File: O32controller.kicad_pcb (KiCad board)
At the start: 4 copper layers, 27 x 27 mm, 81 parts, among them J1 SWD, J10 3V3, J11 GND, J12 I2C/RS485_2, J2 BATT+, J3 BATT-, J4 Motor Connection, J5 Motor Connection, J6 Motor Connection, J7 BATT+, J8 BATT-, J9 I2C/RS485_1, Q1 CSD88584Q5DCT, Q2 CSD88584Q5DCT, Q3 CSD88584Q5DCT, SW1 RESET, U1 MA702GQ-P, U2 STSPIN32F0A, U3 THVD1420DRLR

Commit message: woohoo everything connected, no drc err
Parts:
- added R30: 27.4k, Resistor_SMD:R_0402_1005Metric, B.Cu at (47.9, 55.3)
- added R31: 27.4k, Resistor_SMD:R_0402_1005Metric, B.Cu at (45.8, 55.6)
- added R32: 27.4k, Resistor_SMD:R_0402_1005Metric, B.Cu at (43.7, 49.2)
- added R33: 27.4k, Resistor_SMD:R_0402_1005Metric, B.Cu at (43.7, 48.3)
- added R34: 27.4k, Resistor_SMD:R_0402_1005Metric, B.Cu at (42.1, 46.2)
- added R35: 27.4k, Resistor_SMD:R_0402_1005Metric, B.Cu at (43.1, 46.2)
- D1: value SBA0540Q -> SDM2U30CSP; footprint Diode_SMD:D_DFN2L -> O32controller:SDM2U30CSP-7
- D5, D6: value PMEG4010ESB -> SDM2U30CSP
- J10, J11: footprint Connector_Wire:SolderWire-0.1sqmm_1x01_D0.4mm_OD1mm -> O32controller:SolderWire-Actual_1x01_D1.25mm_OD_2.3mm
- NT4, NT5, TP2, U3: moved to B.Cu
- R1, R5, R9: value WFCP06124L000FE66 0.004R -> WSLF25122L000FEB 0.002R
- moved R29 25.3 mm to (38.5, 42.3), turned to 90 degrees
- moved TP2 23.1 mm to (44.0, 58.4), turned to 180 degrees
- moved NT4 20.7 mm to (43.0, 43.6), turned to 180 degrees
- moved NT5 19.6 mm to (43.0, 42.6), turned to 180 degrees
- moved D6 18.3 mm to (39.4, 45.9), turned to 180 degrees
- moved D5 17.8 mm to (37.5, 47.5), turned to 90 degrees
- moved J10 15.7 mm to (41.5, 59.5)
- moved J11 15.6 mm to (41.5, 62.1)
- moved D2 10.8 mm to (53.9, 37.9), turned to -90 degrees
- moved U3 6.26 mm to (42.0, 50.9), turned to 90 degrees
- moved J9 5.80 mm to (39.5, 43.1)
- moved D1 5.03 mm to (40.7, 55.2), turned to -90 degrees
- moved D3 4.99 mm to (37.2, 45.0), turned to 90 degrees
- moved J12 4.65 mm to (39.5, 48.5)
- moved R28 3.52 mm to (38.5, 44.4), turned to 90 degrees
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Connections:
- net /USART1_DE renamed /USART_DE
- net Net-(D3-Pad2) renamed /Red_Anode
- net Net-(D4-Pad1) renamed /Green_Cathode
- net USART1_TX renamed USART_TX
- U3 pad 1: /USART1_RX -> /USART_RX
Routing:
- net +3.3V: track 2.68 -> 61.6 mm, vias 0 -> 7
- net GND: track 11.8 -> 37.0 mm, vias 12 -> 33
- net VBUS: track 1.62 -> 24.2 mm, vias 2 -> 4
- net SWD_IO: track 1.81 -> 15.6 mm
- net /RS485_B: track 0.00 -> 12.5 mm, vias 0 -> 2
- net USART_TX: track 0.00 -> 11.8 mm, vias 0 -> 1
- net /NRST: track 0.00 -> 11.8 mm, vias 0 -> 2
- net SWD_CLK: track 0.66 -> 12.2 mm
- net /RS485_A: track 0.00 -> 10.9 mm
- net /SW_3.3: track 0.00 -> 8.05 mm
- net /LED_STATUS: track 0.00 -> 6.93 mm
- net /USART_RX: track 1.11 -> 6.92 mm
- net I2C_SCL: track 0.00 -> 5.63 mm
- net /BUS_SENSE: track 0.00 -> 5.48 mm, vias 0 -> 1
- net /OP_V_O: track 3.31 -> 8.47 mm
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- added copper zone on In1.Cu, net GND

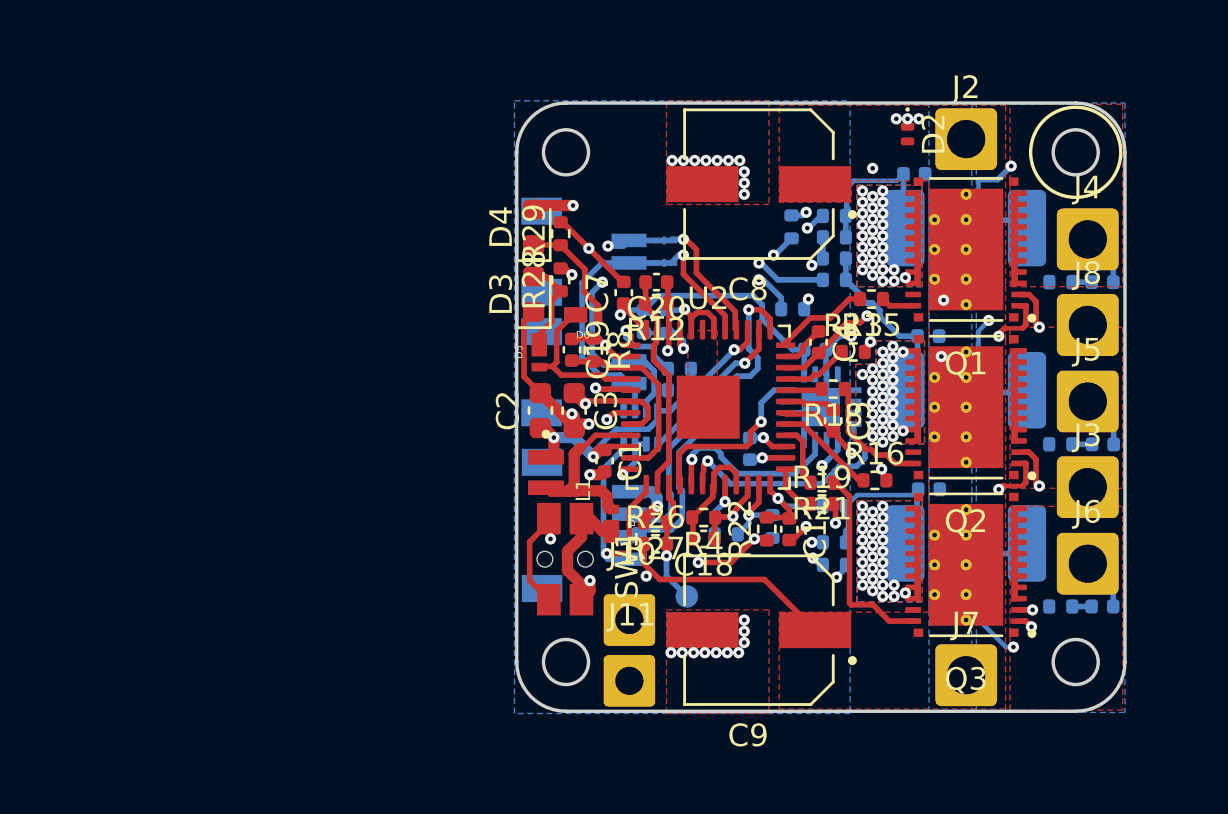
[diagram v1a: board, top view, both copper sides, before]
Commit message: choose led, tvs, start on silkscreen
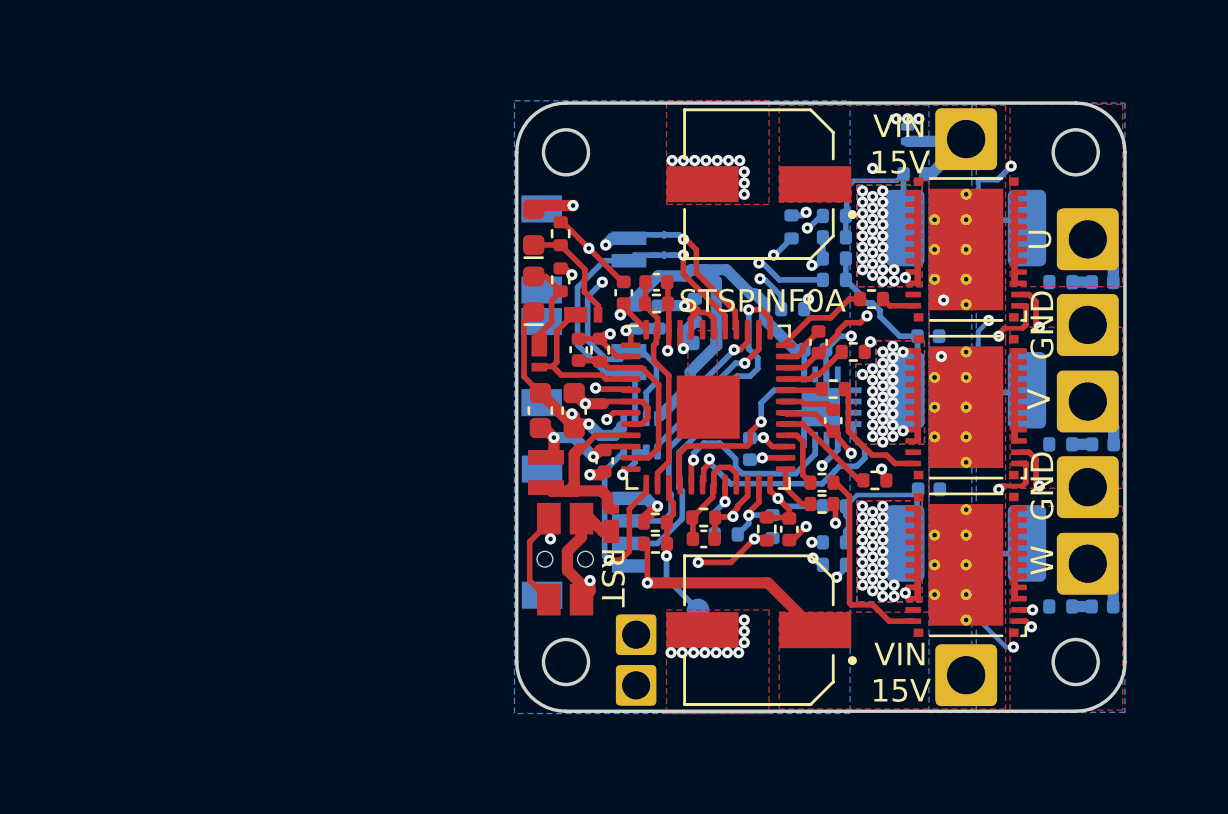
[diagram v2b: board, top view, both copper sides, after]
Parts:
- D2: moved to B.Cu
- J10, J11: footprint O32controller:SolderWire-Actual_1x01_D1.25mm_OD_2.3mm -> O32controller:SolderWire-Actual_1x01_D1.25mm_OD_1.8mm
- Q1, Q2, Q3: value CSD88584Q5DCT -> DMM0022A
- U1: value MA702GQ-P -> QFN-3x3_MA702_MNP
- moved R32 3.77 mm to (41.8, 46.0), turned to 90 degrees
- moved R34 2.86 mm to (44.9, 47.1), turned to 0 degrees
- moved R33 2.48 mm to (42.8, 46.0), turned to -90 degrees
- moved R35 1.35 mm to (44.4, 45.7)
- moved BUS_SENSE 0.78 mm to (44.5, 59.0)
- moved J10 0.72 mm to (41.8, 60.1)
- moved J12 0.45 mm to (39.5, 48.0)
- moved J11 0.36 mm to (41.8, 62.4)
- moved NT4 0.35 mm to (43.0, 43.2)
- moved U3 0.35 mm to (42.0, 51.2)
- moved R8 0.30 mm to (40.2, 47.5)
- moved C19 0.30 mm to (39.2, 47.5)
- moved J1 0.30 mm to (41.5, 55.5)
- moved NT5 0.25 mm to (43.0, 42.4)
- moved J9 0.10 mm to (39.5, 43.0)
- renumbered TP2 to BUS_SENSE, SW1 to RST, U2 to STSPINF0A
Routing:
- net VBUS: track 24.2 -> 30.0 mm
- net +3.3V: track 61.6 -> 64.6 mm
- net GND: track 37.0 -> 39.9 mm
- net /OP_V_P: track 15.0 -> 12.5 mm
- net /Motor phase U/Motor: track 3.98 -> 2.37 mm
- net USART_TX: track 11.8 -> 10.6 mm
- net /RS485_B: track 12.5 -> 13.4 mm
- net /OP_W_P: track 17.0 -> 16.2 mm
- net /BUS_SENSE: track 5.48 -> 6.29 mm
- net /RS485_A: track 10.9 -> 11.6 mm
- net /OC_COMP: track 18.0 -> 18.6 mm
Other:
- board text added: "GND"
- board text added: "U"
- board text added: "V"
- board text added: "VIN 15V"
- board text added: "W"

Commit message: silkscreen pretty much done
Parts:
- U1: value QFN-3x3_MA702_MNP -> MA702
- renumbered U3 to RS485, BUS_SENSE to SNS
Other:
- board text added: "+"
- board text added: "-"
- board text added: "2mΩ 5W"
- board text added: "3.3"
- board text added: "CLK"
- board text added: "I2C,RS485"
- board text added: "IO"
- board text added: "M2"
- board text added: "SCL,B"
- board text added: "SDA,A"
- board text added: "TX"
- board text added: "VIN"
- board text added: "VIN: 7-15V"
- board text added: "Ø32"
- board text removed: "VIN 15V"

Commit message: finish, generate gerbers
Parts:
- added C21: 1nF, Capacitor_SMD:C_0402_1005Metric, B.Cu at (45.8, 56.6)
- Q1, Q2, Q3: value DMM0022A -> CSD88584Q5DCT
- R26: value 40k -> 41.2k
- renumbered RS485 to U3
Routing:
- net /BUS_SENSE: track 6.29 -> 8.69 mm
- net /Motor phase U/Sense_N: track 15.1 -> 14.5 mm, vias 3 -> 2
- net GND: track 39.9 -> 39.6 mm, vias 33 -> 51
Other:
- board text added: "16AWG"
- board text added: "3.3V"
- board text added: "JST"
- board text added: "SH"
- board text added: "[1/6/23]"
- board text added: "v2"
- board text removed: "3.3"

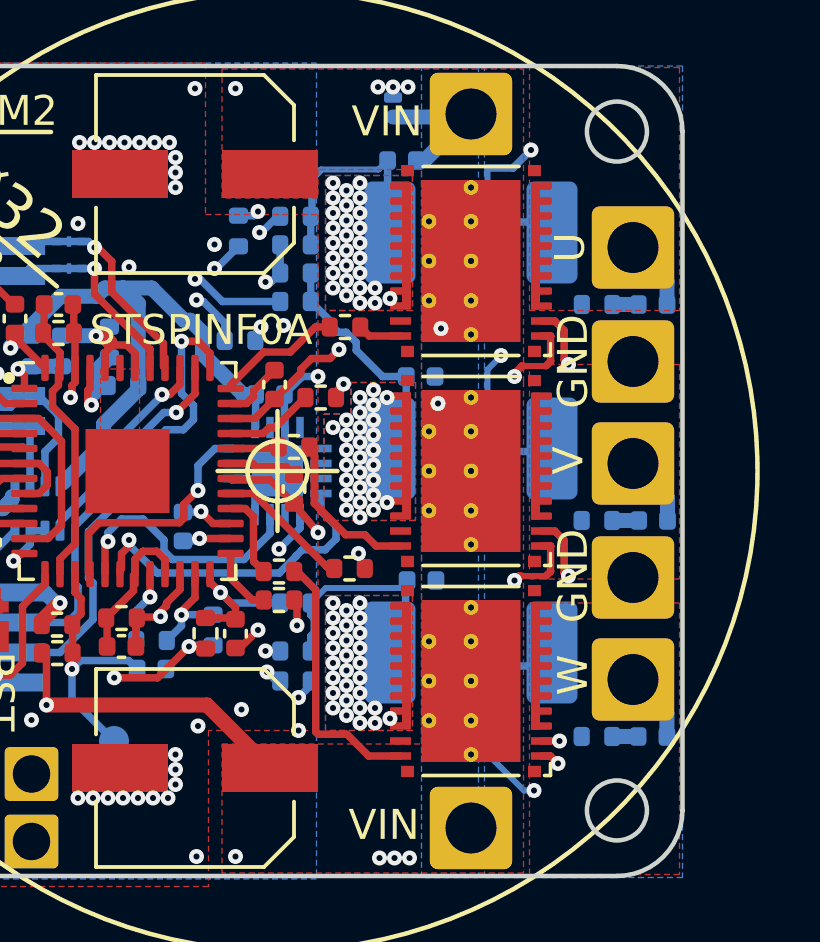
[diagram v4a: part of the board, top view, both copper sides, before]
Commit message: fix mosfet soldermask
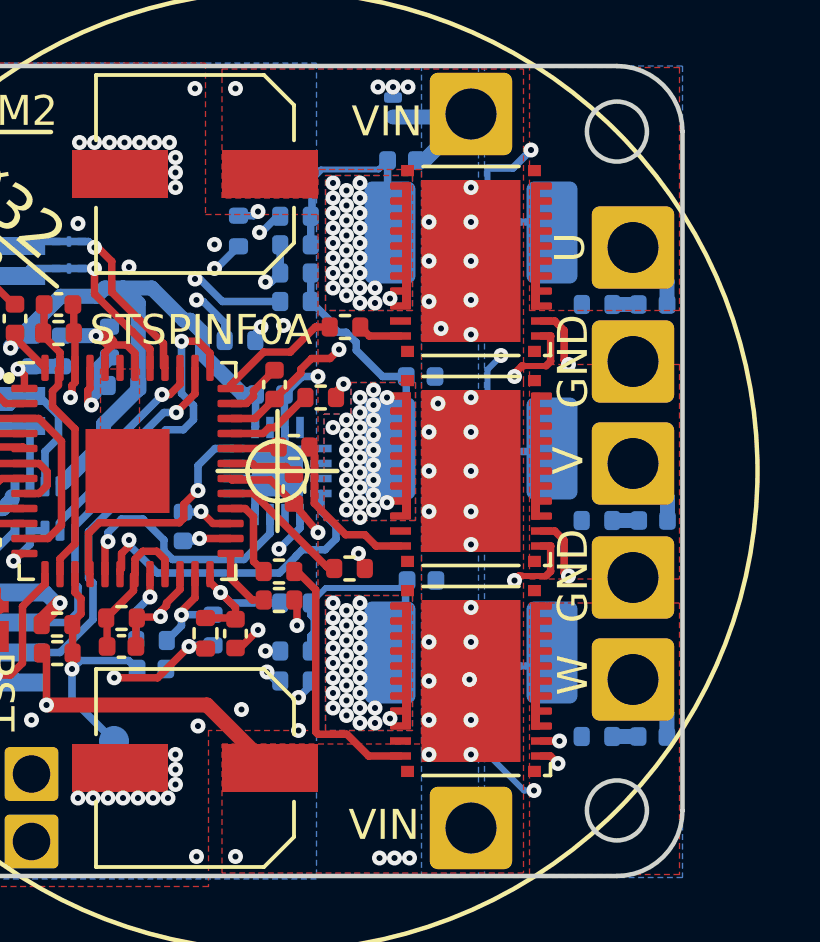
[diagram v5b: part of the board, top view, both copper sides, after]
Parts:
- Q1, Q2, Q3: value CSD88584Q5DCT -> DMM0022A
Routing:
- net VBUS: vias 4 -> 29

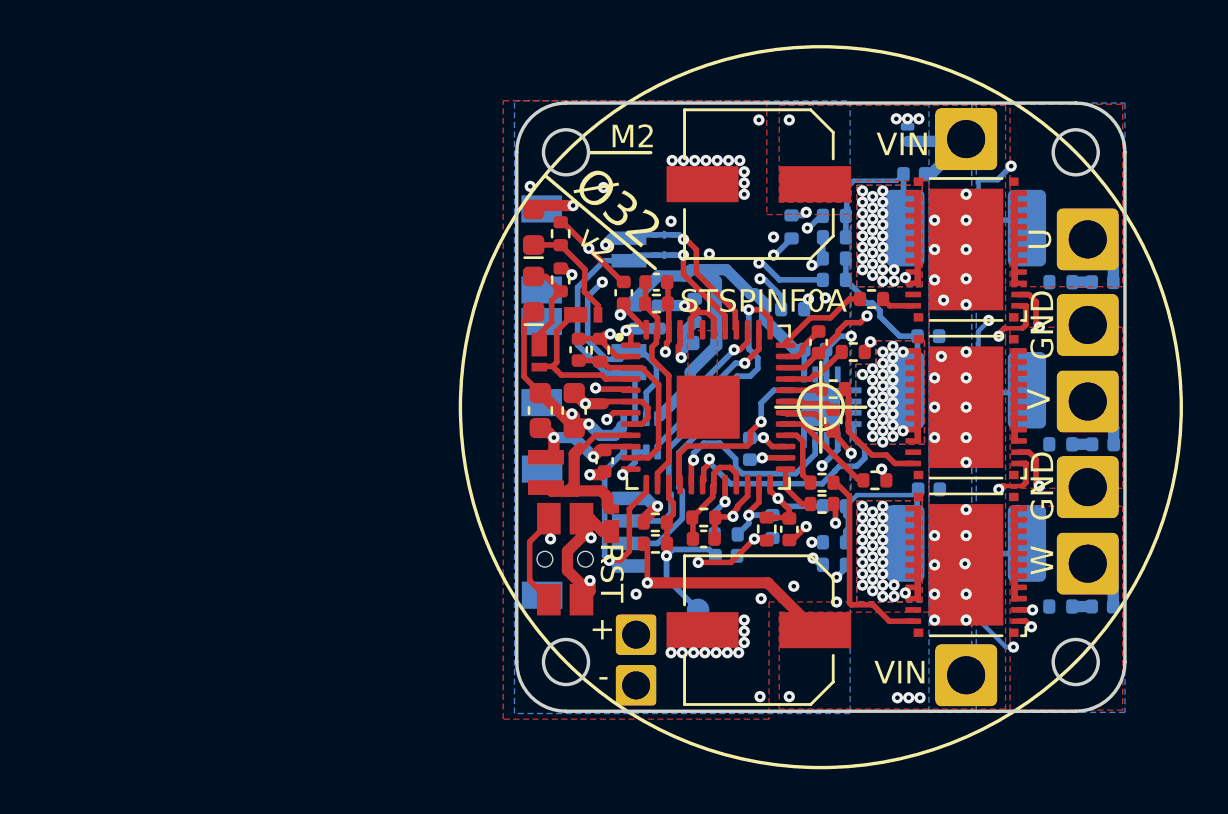
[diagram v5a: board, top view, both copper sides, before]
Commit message: clean up v2, fix libraries, netties, fix TVS dir
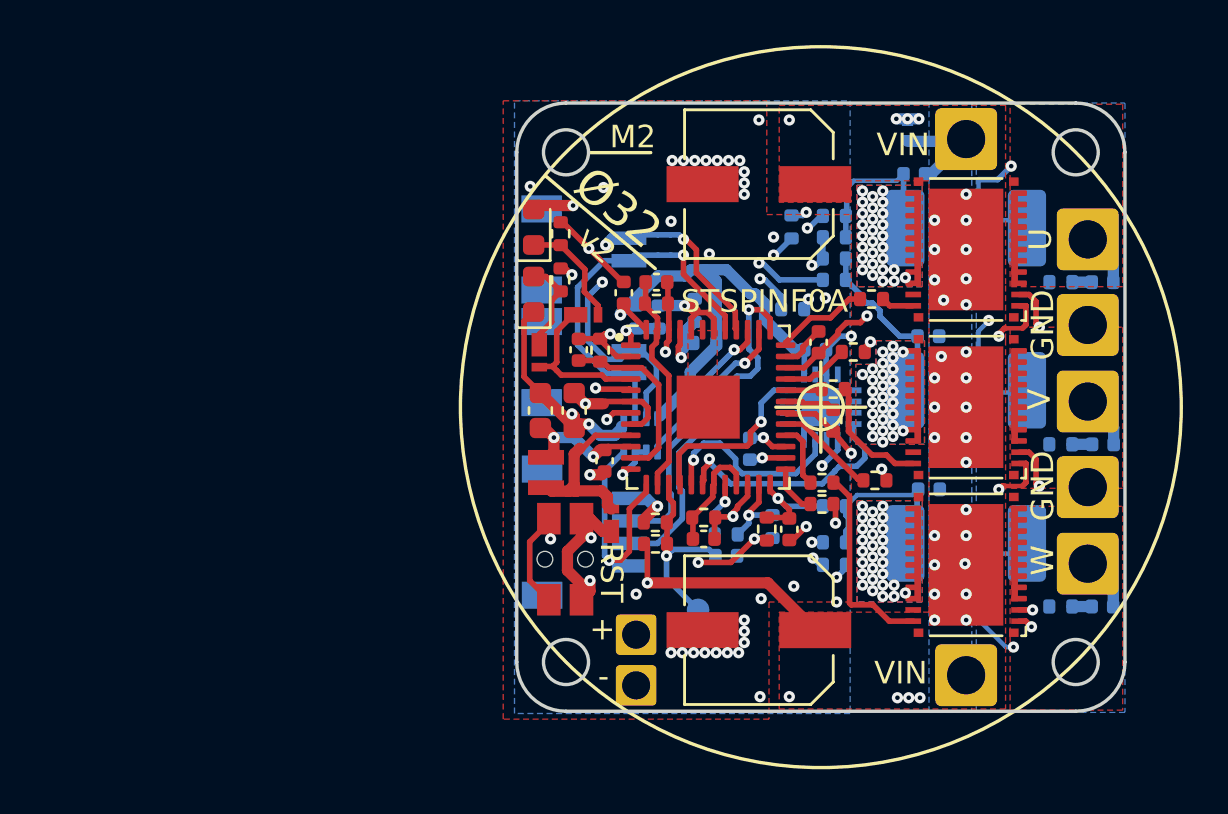
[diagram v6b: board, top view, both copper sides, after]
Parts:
- removed D2: ESDA17P20-1F2, Diode_SMD:D_0402_CSP
- added CR1: ESDA17P20-1F2, O32controller:SMT2_0P91X0P63_STM-L, B.Cu at (53.9, 37.7)
- NT1, NT2, NT3, NT4, NT5: footprint NetTie:NetTie-small -> O32controller:NetTie-2_SMD_Pad0.25mm
- R1, R5, R9: footprint Resistor_SMD:R_Shunt_2512_6332Metric -> O32controller:R_Shunt_2512_6332Metric
- U1: value MA702 -> QFN-3x3_MA702_MNP
- moved NT3 0.45 mm to (57.4, 56.5)
- moved NT1 0.40 mm to (57.4, 41.7)
- moved NT2 0.35 mm to (57.4, 49.4)
- renumbered RST to SW1, SNS to TP2, STSPINF0A to U2
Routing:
- net GND: track 39.6 -> 45.4 mm
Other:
- board text added: "MA702"
- board text added: "RST"
- board text added: "SNS"
- board text added: "STSPINF0A"
- board text added: "locked"
- board text removed: "2mΩ 5W"

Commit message: remove motor conn from ibom, reannotate tvs diode
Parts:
- Q1, Q2, Q3: value DMM0022A -> CSD88584Q5DCT
- U1: value QFN-3x3_MA702_MNP -> MA702GQ-P
- renumbered CR1 to D2
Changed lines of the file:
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@@
     (property "Sheetfile" "motorphase.kicad_sch")
     (property "Sheetname" "Motor phase V")
+    (property "exclude_from_bom" "")
     (property "ki_description" "Generic connector, single row, 01x01, script generated (kicad-library-utils/schlib/autogen/connector/)")
     (property "ki_keywords" "connector")
-    (attr exclude_from_pos_files)
+    (attr exclude_from_pos_files exclude_from_bom)
     (fp_text reference "J5" (at 0 -2.286) (layer "F.SilkS") hide
         (effects (font (size 1 1) (thickness 0.15)) (justify mirror))
@@
         (effects (font (size 1 1) (thickness 0.15)))
     )
-    (fp_text value "DMM0022A" (at 0 5.08) (layer "F.Fab")
+    (fp_text value "CSD88584Q5DCT" (at 0 5.08) (layer "F.Fab")
         (effects (font (size 1 1) (thickness 0.15)))
     )
@@
         (effects (font (size 1 1) (thickness 0.15)))
     )
-    (fp_text value "DMM0022A" (at 0 5.08) (layer "F.Fab")
+    (fp_text value "CSD88584Q5DCT" (at 0 5.08) (layer "F.Fab")
         (effects (font (size 1 1) (thickness 0.15)))
     )
@@
     (property "Sheetfile" "motorphase.kicad_sch")
     (property "Sheetname" "Motor phase U")
+    (property "exclude_from_bom" "")
     (property "ki_description" "Generic connector, single row, 01x01, script generated (kicad-library-utils/schlib/autogen/connector/)")
     (property "ki_keywords" "connector")
-    (attr exclude_from_pos_files)
+    (attr exclude_from_pos_files exclude_from_bom)
     (fp_text reference "J4" (at 0 -2.286) (layer "F.SilkS") hide
         (effects (font (size 1 1) (thickness 0.15)) (justify mirror))
@@
         (effects (font (size 1 1) (thickness 0.15)))
     )
-    (fp_text value "DMM0022A" (at 0 5.08) (layer "F.Fab")
+    (fp_text value "CSD88584Q5DCT" (at 0 5.08) (layer "F.Fab")
         (effects (font (size 1 1) (thickness 0.15)))
     )
@@
     (property "Sheetfile" "motorphase.kicad_sch")
     (property "Sheetname" "Motor phase W")
+    (property "exclude_from_bom" "")
     (property "ki_description" "Generic connector, single row, 01x01, script generated (kicad-library-utils/schlib/autogen/connector/)")
     (property "ki_keywords" "connector")
-    (attr exclude_from_pos_files)
+    (attr exclude_from_pos_files exclude_from_bom)
     (fp_text reference "J6" (at 0 -2.286) (layer "F.SilkS") hide
         (effects (font (size 1 1) (thickness 0.15)) (justify mirror))
@@
         (effects (font (size 1 1) (thickness 0.15)) (justify mirror))
     )
-    (fp_text value "QFN-3x3_MA702_MNP" (at 0 -2.6) (layer "B.SilkS") hide
+    (fp_text value "MA702GQ-P" (at 0 -2.6) (layer "B.SilkS") hide
         (effects (font (size 1 1) (thickness 0.15)) (justify mirror))
     )
@@
     (at 53.85 37.71865 90)
     (tags "ESDA17P20-1F2 ")
+    (property "MP" "ESDA17P20-1F2")
     (property "Sheetfile" "O32controller.kicad_sch")
     (property "Sheetname" "")
     (property "ki_keywords" "ESDA17P20-1F2")
     (attr smd)
-    (fp_text reference "CR1" (at 0 0 270 unlocked) (layer "B.SilkS") hide
+    (fp_text reference "D2" (at 0 0 270 unlocked) (layer "B.SilkS") hide
         (effects (font (size 1 1) (thickness 0.15)) (justify mirror))
     )
